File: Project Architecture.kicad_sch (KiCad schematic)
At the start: 29 parts, among them J1 Screw_Terminal_01x04

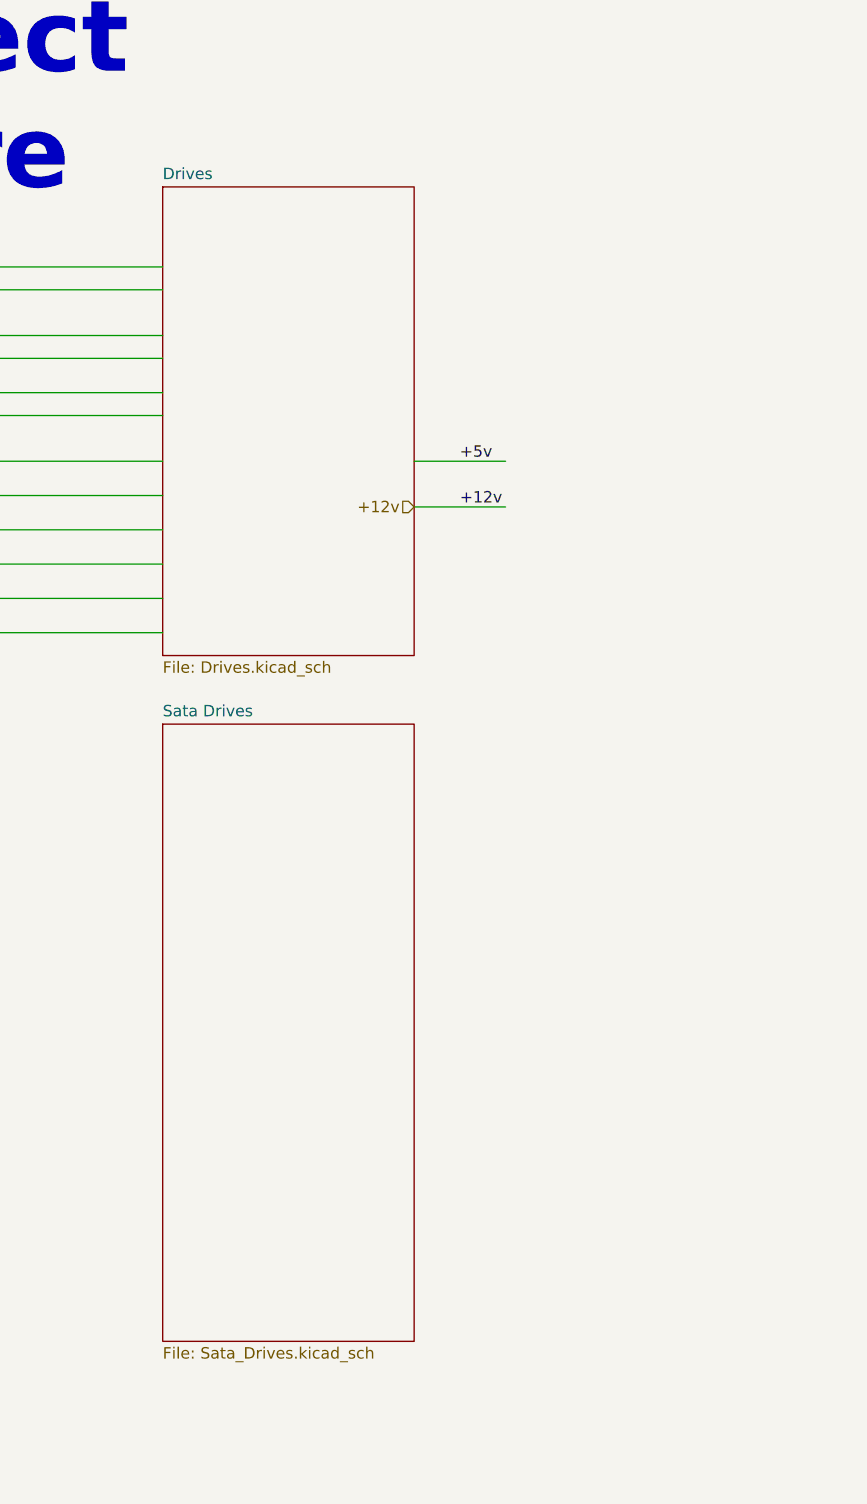
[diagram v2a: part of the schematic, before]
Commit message: Digital Reg with multiple v
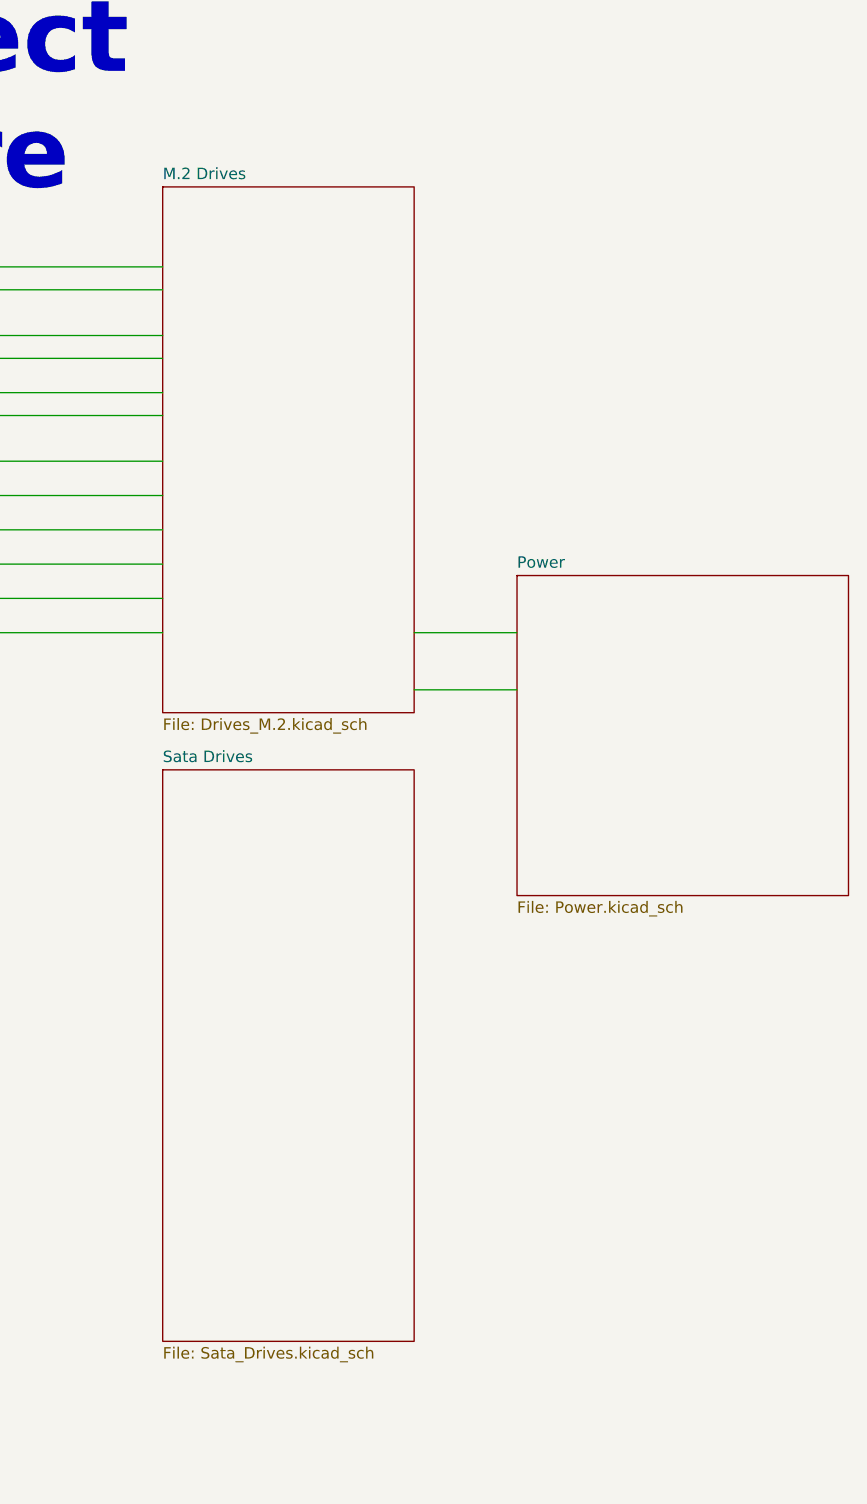
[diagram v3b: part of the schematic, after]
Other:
- sheet Drives renamed M.2 Drives
- added sheet Power (Power.kicad_sch)
- sheet M.2 Drives: file Drives.kicad_sch -> Drives_M.2.kicad_sch
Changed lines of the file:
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@@
 		)
 	)
-	(wire
+	(polyline
 		(pts
-			(xy 287.02 68.58) (xy 297.18 68.58)
+			(xy 35.56 30.48) (xy 35.56 41.91)
 		)
 		(stroke
@@
 		)
 	)
-	(polyline
+	(wire
 		(pts
-			(xy 35.56 30.48) (xy 35.56 41.91)
+			(xy 46.99 71.12) (xy 52.07 71.12)
 		)
 		(stroke
@@
 	(wire
 		(pts
-			(xy 46.99 71.12) (xy 52.07 71.12)
+			(xy 287.02 88.9) (xy 298.45 88.9)
 		)
 		(stroke
@@
 	(wire
 		(pts
+			(xy 287.02 82.55) (xy 298.45 82.55)
+		)
+		(stroke
+			(width 0)
+			(type default)
+		)
+	)
+	(wire
+		(pts
 			(xy 177.8 161.29) (xy 177.8 176.53)
 		)
@@
 	(wire
 		(pts
-			(xy 287.02 63.5) (xy 297.18 63.5)
-		)
-		(stroke
-			(width 0)
-			(type default)
-		)
-	)
-	(wire
-		(pts
 			(xy 115.57 78.74) (xy 125.73 78.74)
 		)
@@
 		)
 	)
-	(label "+5v"
-		(at 292.1 63.5 0)
-		(effects
-			(font
-				(size 1.27 1.27)
-			)
-			(justify left bottom)
-		)
-	)
 	(label "CM5+5v"
 		(at 233.68 199.39 0)
@@
 		)
 	)
-	(label "+12v"
-		(at 292.1 68.58 0)
-		(effects
-			(font
-				(size 1.27 1.27)
-			)
-			(justify left bottom)
-		)
-	)
 	(label "+5v"
 		(at 135.89 71.12 0)
@@
 		)
 	)
-	(hierarchical_label "+12v"
-		(shape input)
-		(at 287.02 68.58 180)
-		(effects
-			(font
-				(size 1.27 1.27)
-			)
-			(justify right)
-		)
-	)
 	(symbol
 		(lib_id "Mechanical:MountingHole")
@@
 	(sheet
 		(at 259.08 33.02)
-		(size 27.94 52.07)
+		(size 27.94 58.42)
 		(exclude_from_sim no)
 		(in_bom yes)
@@
 			(color 255 255 255 0.0000)
 		)
-		(property "Sheetname" "Drives"
+		(property "Sheetname" "M.2 Drives"
 			(at 259.08 32.3086 0)
 			(effects
@@
 			)
 		)
-		(property "Sheetfile" "Drives.kicad_sch"
-			(at 259.08 85.6744 0)
+		(property "Sheetfile" "Drives_M.2.kicad_sch"
+			(at 259.08 92.0244 0)
+			(effects
+				(font
+					(size 1.27 1.27)
+				)
+				(justify left top)
+			)
+		)
+		(instances
+			(project "CM5 Nas"
+				(path "/0650c7a8-acba-429c-9f8e-eec0baf0bc1c/fede4c36-00cc-4d3d-b71c-5243ba232202"
+					(page "7")
+				)
+			)
+		)
+	)
+	(sheet
+		(at 298.45 76.2)
+		(size 36.83 35.56)
+		(exclude_from_sim no)
+		(in_bom yes)
+		(on_board yes)
+		(dnp no)
+		(fields_autoplaced yes)
+		(stroke
+			(width 0.1524)
+			(type solid)
+		)
+		(fill
+			(color 0 0 0 0.0000)
+		)
+		(property "Sheetname" "Power"
+			(at 298.45 75.4884 0)
+			(effects
+				(font
+					(size 1.27 1.27)
+				)
+				(justify left bottom)
+			)
+		)
+		(property "Sheetfile" "Power.kicad_sch"
+			(at 298.45 112.3446 0)
 			(effects
 				(font
@@
 	)
 	(sheet
-		(at 259.08 92.71)
-		(size 27.94 68.58)
+		(at 259.08 97.79)
+		(size 27.94 63.5)
 		(exclude_from_sim no)
 		(in_bom yes)
@@
 		)
 		(property "Sheetname" "Sata Drives"
-			(at 259.08 91.9984 0)
+			(at 259.08 97.0784 0)
 			(effects
 				(font

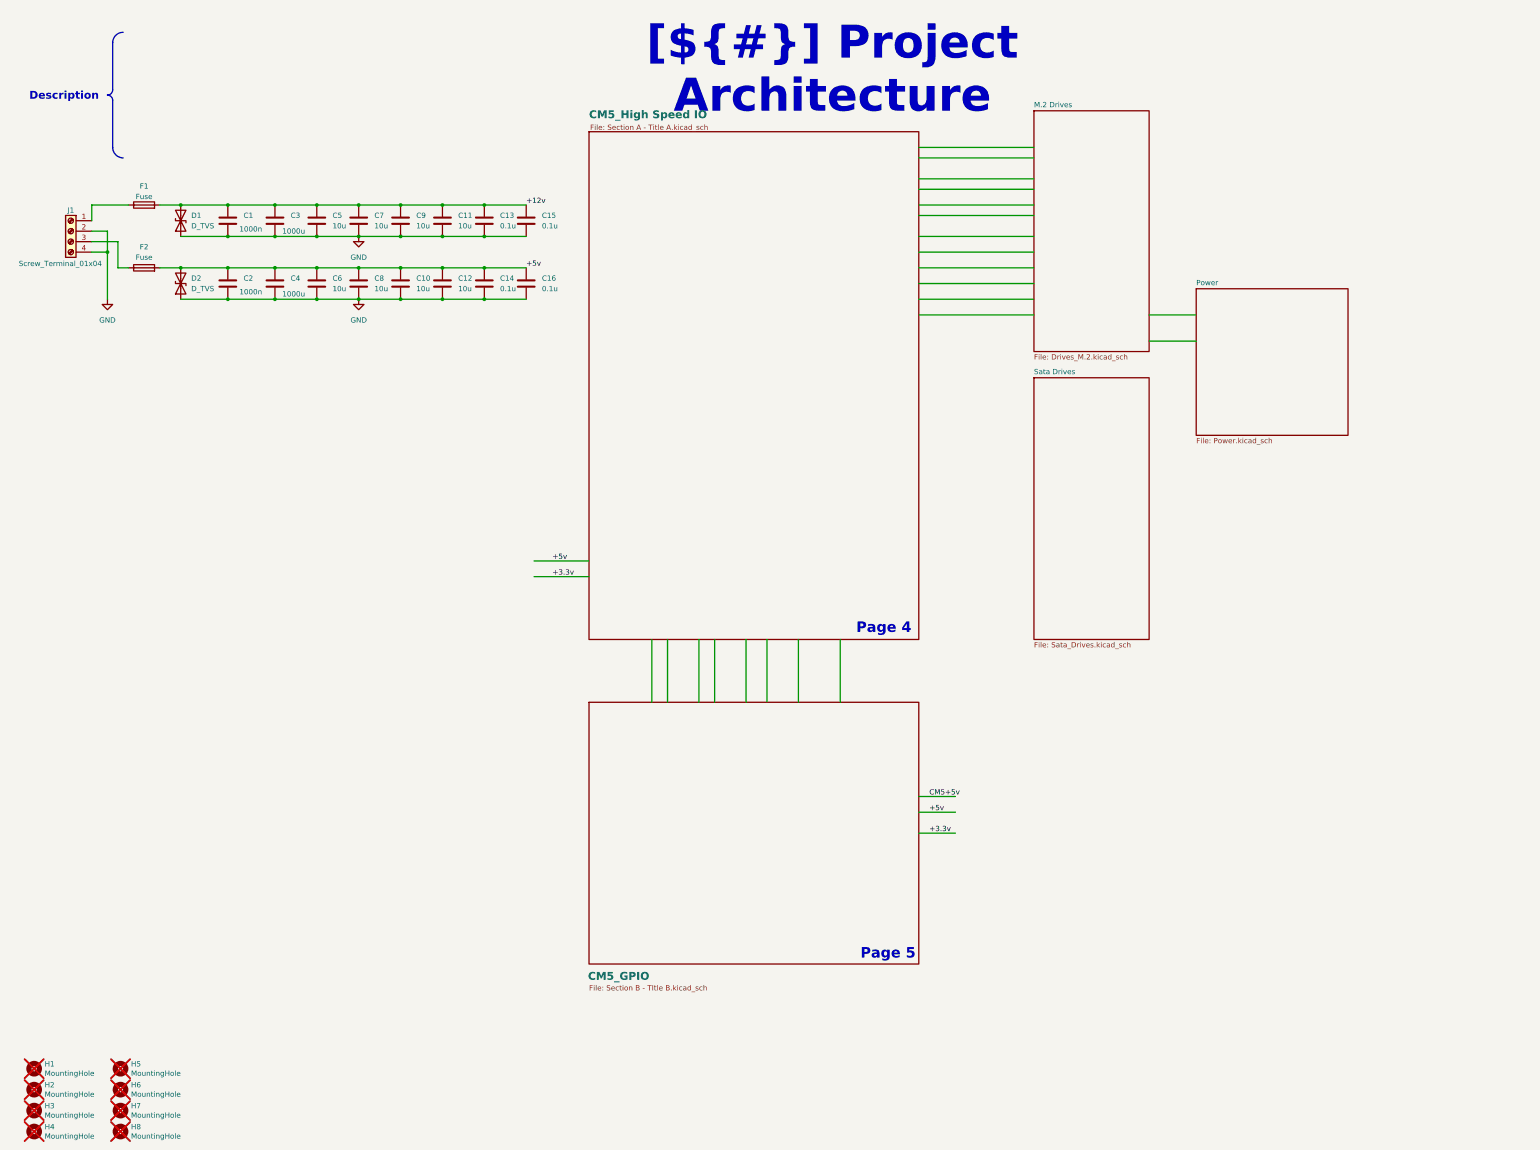
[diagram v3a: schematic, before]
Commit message: Drives moved
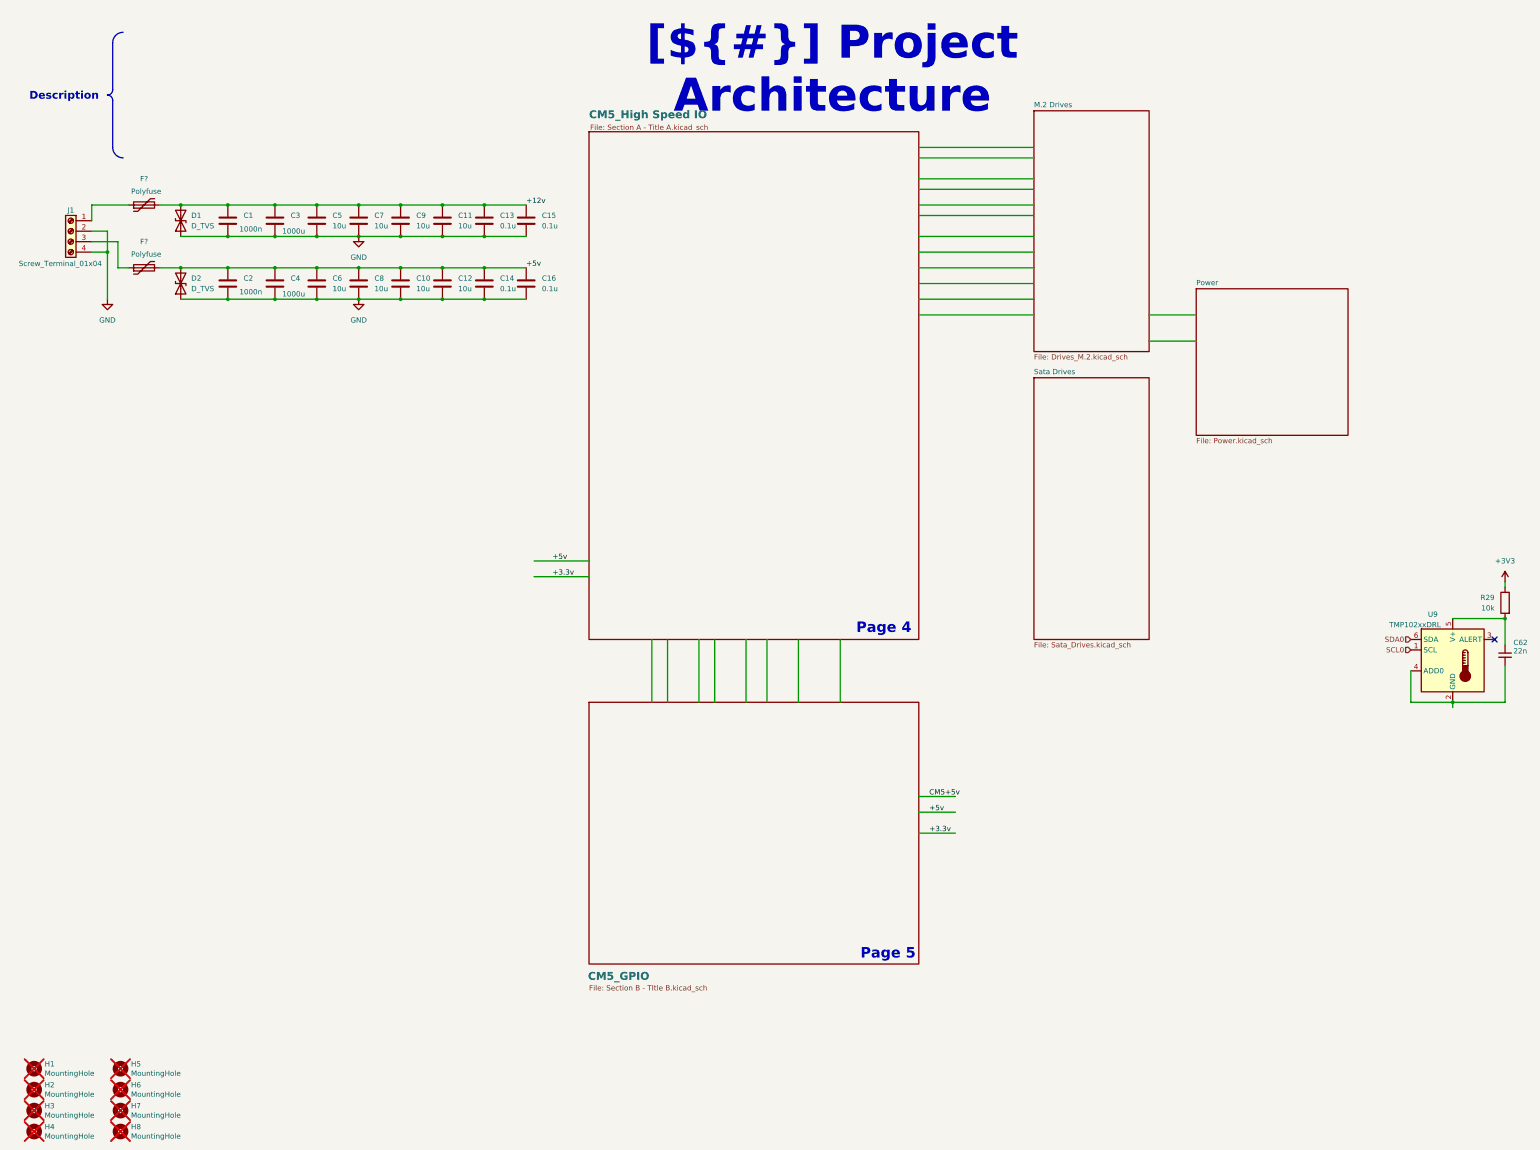
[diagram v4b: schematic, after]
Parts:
- removed F1, F2: Fuse, symbol Device:Fuse
- added C62: 22n, symbol Device:C_Small
- added F? (x2): Polyfuse, symbol Device:Polyfuse
- added R29: 10k, symbol Device:R
- added U9: TMP102xxDRL, Package_TO_SOT_SMD:SOT-563, symbol Sensor_Temperature:TMP102xxDRL
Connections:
- net +12v: now also F?.2
- net +5v: now also F?.2
- net at J1.1 (Pin_1): now also F?.1
- net at J1.3 (Pin_3): now also F?.1
- new net: C62.1, R29.2, U9.5 (V+)
- new net: C62.2, U9.2 (GND), U9.4 (ADD0)
- new net +3V3: R29.1
- new net SCL0: U9.1 (SCL)
- new net SDA0: U9.6 (SDA)
- no-connect marks 0 -> 1

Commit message: Sheet name edit and changed to net labels
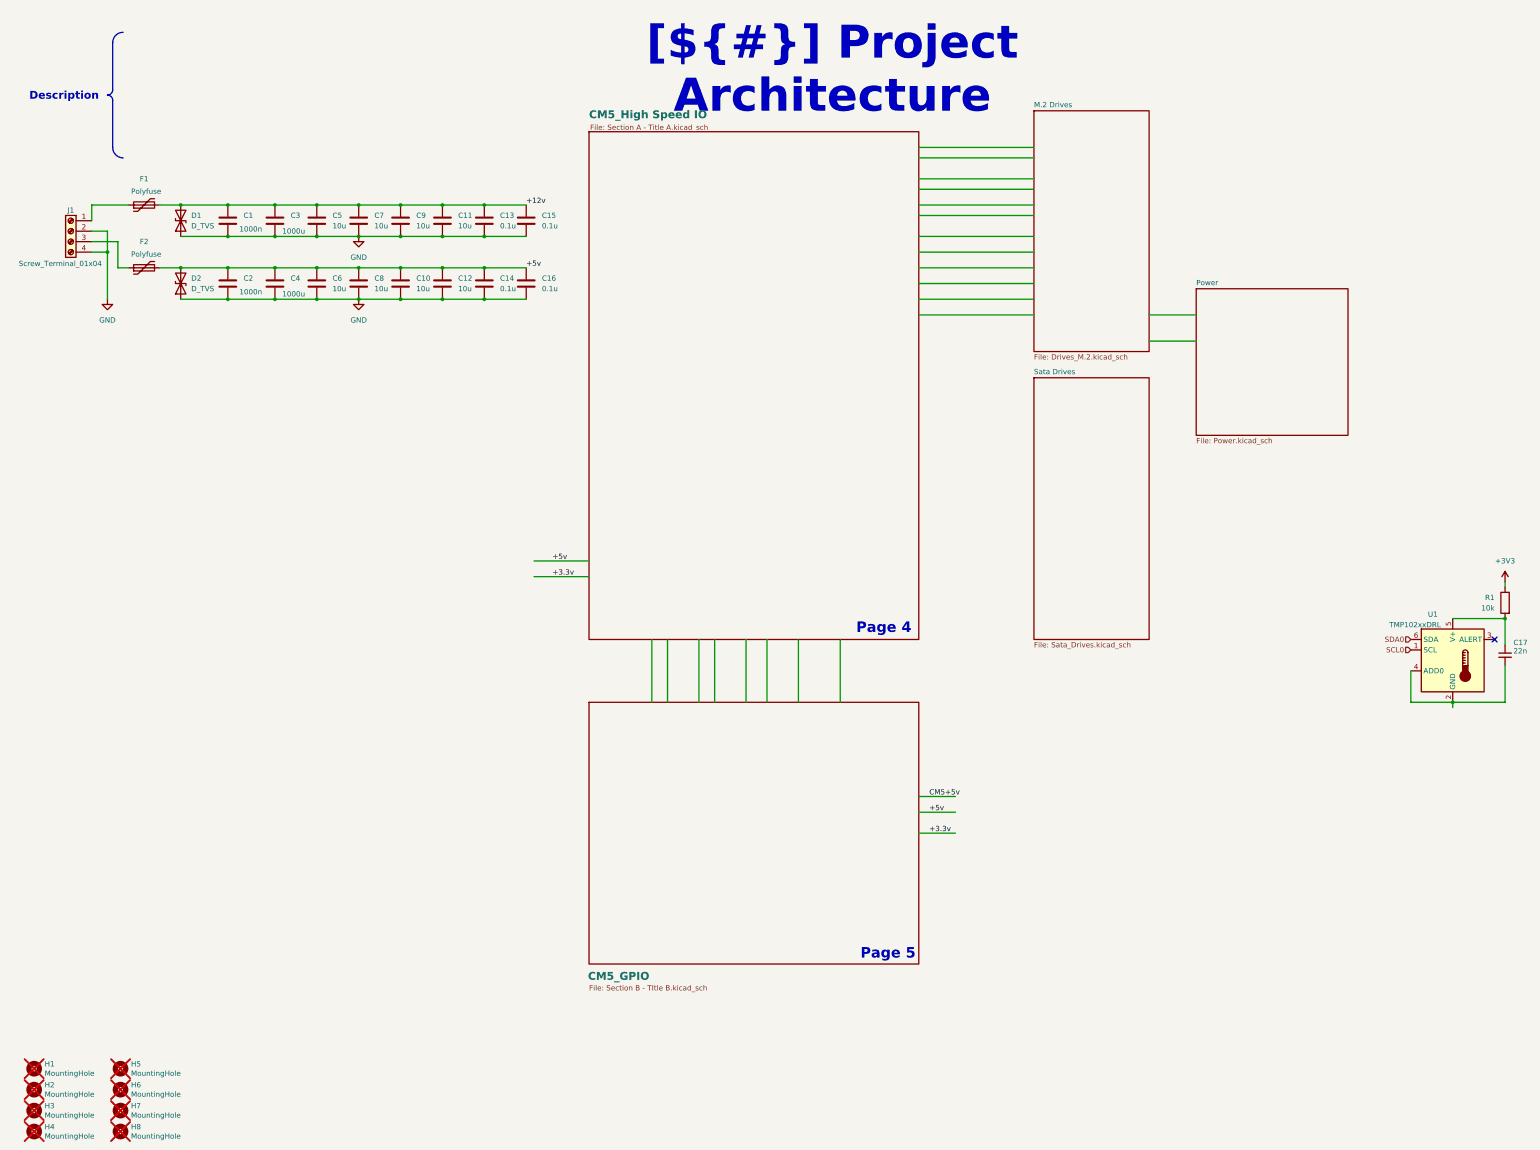
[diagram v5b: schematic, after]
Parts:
- gave numbers to parts that had none: 2
- renumbered C62 to C17, R29 to R1, U9 to U1
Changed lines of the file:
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@@
 		(on_board yes)
 		(dnp no)
-		(property "Reference" "R29"
+		(property "Reference" "R1"
 			(at 370.84 151.1299 0)
 			(effects
@@
 			(project "CM5 Nas"
 				(path "/0650c7a8-acba-429c-9f8e-eec0baf0bc1c/fede4c36-00cc-4d3d-b71c-5243ba232202"
-					(reference "R29")
+					(reference "R1")
 					(unit 1)
 				)
@@
 		(dnp no)
 		(fields_autoplaced yes)
-		(property "Reference" "#PWR053"
+		(property "Reference" "#PWR04"
 			(at 373.38 151.13 0)
 			(effects
@@
 			(project "CM5 Nas"
 				(path "/0650c7a8-acba-429c-9f8e-eec0baf0bc1c/fede4c36-00cc-4d3d-b71c-5243ba232202"
-					(reference "#PWR053")
+					(reference "#PWR04")
 					(unit 1)
 				)
@@
 		(on_board yes)
 		(dnp no)
-		(property "Reference" "C62"
+		(property "Reference" "C17"
 			(at 375.412 162.052 0)
 			(effects
@@
 			(project "CM5 Nas"
 				(path "/0650c7a8-acba-429c-9f8e-eec0baf0bc1c/fede4c36-00cc-4d3d-b71c-5243ba232202"
-					(reference "C62")
+					(reference "C17")
 					(unit 1)
 				)
@@
 		(on_board yes)
 		(dnp no)
-		(property "Reference" "U9"
+		(property "Reference" "U1"
 			(at 355.854 155.194 0)
 			(effects
@@
 			(project "CM5 Nas"
 				(path "/0650c7a8-acba-429c-9f8e-eec0baf0bc1c/fede4c36-00cc-4d3d-b71c-5243ba232202"
-					(reference "U9")
+					(reference "U1")
 					(unit 1)
 				)
@@
 		(on_board yes)
 		(dnp no)
-		(property "Reference" "F?"
+		(property "Reference" "F1"
 			(at 43.18 49.53 90)
 			(effects
@@
 			(project "CM5 Nas"
 				(path "/0650c7a8-acba-429c-9f8e-eec0baf0bc1c/fede4c36-00cc-4d3d-b71c-5243ba232202"
-					(reference "F?")
+					(reference "F1")
 					(unit 1)
 				)
@@
 		(on_board yes)
 		(dnp no)
-		(property "Reference" "F?"
+		(property "Reference" "F2"
 			(at 43.18 64.77 90)
 			(effects
@@
 			(project ""
 				(path "/0650c7a8-acba-429c-9f8e-eec0baf0bc1c/fede4c36-00cc-4d3d-b71c-5243ba232202"
-					(reference "F?")
-					(unit 1)
-				)
+					(reference "F2")
+					(unit 1)
+				)
